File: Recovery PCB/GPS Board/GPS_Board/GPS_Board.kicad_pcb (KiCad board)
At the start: 2 copper layers, 85.7 x 50.8 mm, 21 parts, among them J1 XT30-M, J2 XT30-M, U1 Teensy4.1, U2 D24V22F5_VoltageRegulator, U3 LD1117v33, U4 conn_recovery10, U5 conn_recovery10, U6 conn_recovery8

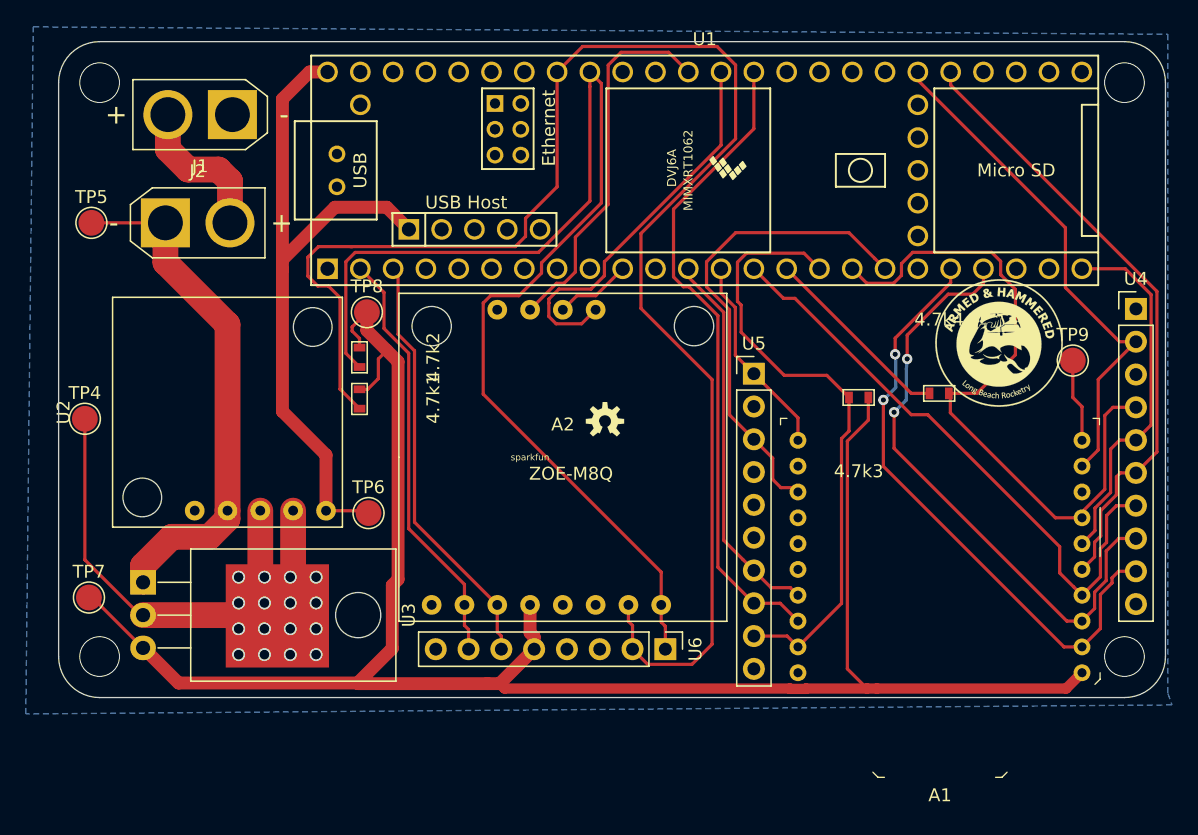
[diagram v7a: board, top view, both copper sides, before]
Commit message: Created SMD Breakout Pins
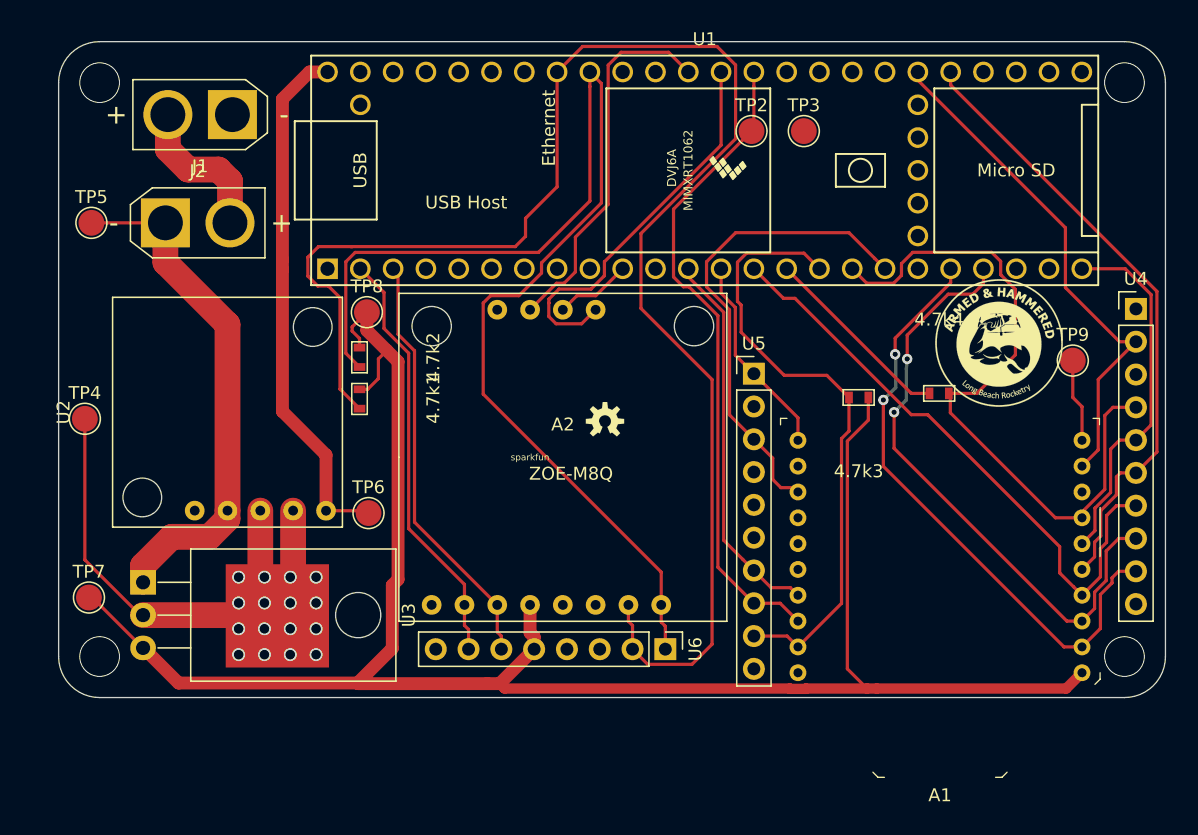
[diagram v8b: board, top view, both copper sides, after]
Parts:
- added TP2: TestPoint, TestPoint:TestPoint_Pad_D2.0mm, F.Cu at (164.8, 67.3)
- added TP3: TestPoint, TestPoint:TestPoint_Pad_D2.0mm, F.Cu at (168.8, 67.3)
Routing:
- net +5V: track 53.2 -> 41.0 mm
- removed copper zone on B.Cu, net GND
